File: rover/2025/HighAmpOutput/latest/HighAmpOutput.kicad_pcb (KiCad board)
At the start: 2 copper layers, 87.8 x 70.7 mm, 24 parts, among them J1 JST2_Pin, U1 EC5_Connector, U11 XT60PM-F, U12 XT60PM-F, U2 HSS-VN7004SLHTR, U3 XT60-F, U4 XT60-F, U5 XT60-F, U6 XT60-F, U7 XT60-F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

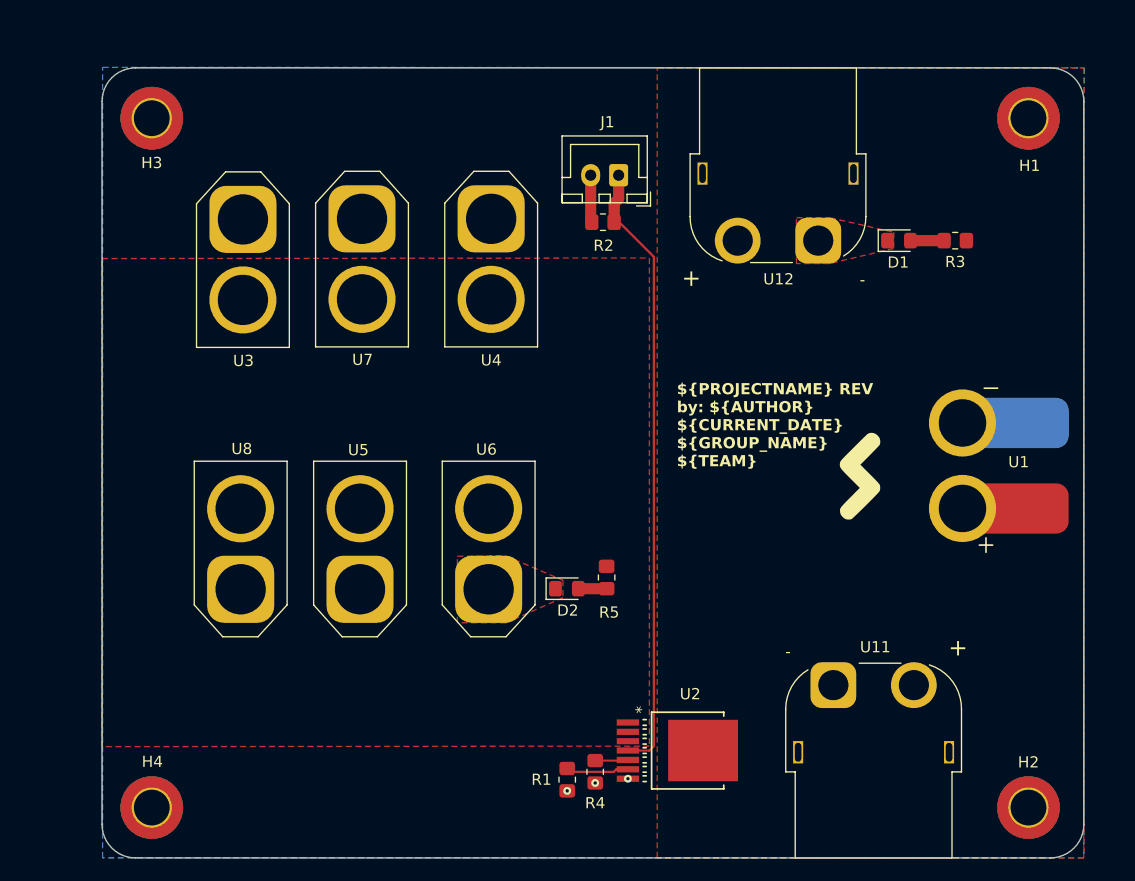
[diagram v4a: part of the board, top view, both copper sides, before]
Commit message: Correction PCB HighAmpOutput
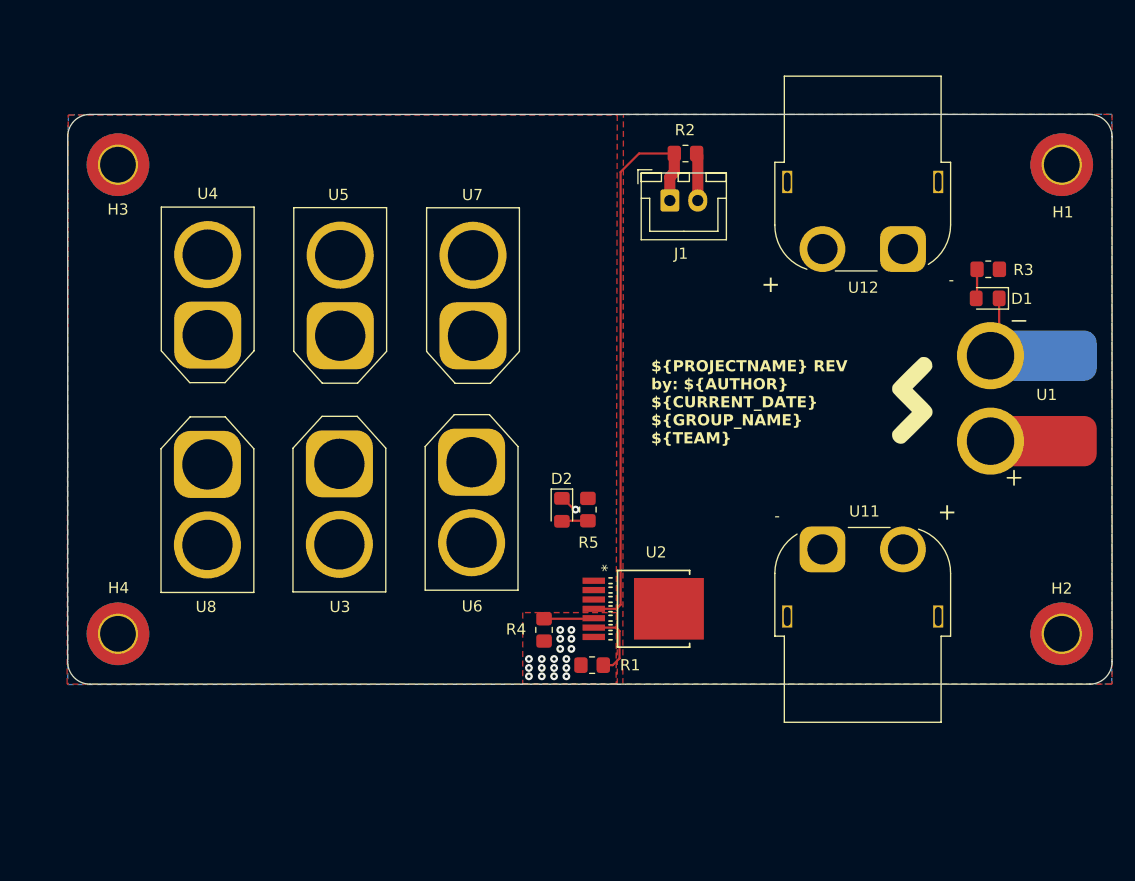
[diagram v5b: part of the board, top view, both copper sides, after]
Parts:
- moved U4 27.4 mm to (64.7, 77.5), turned to 90 degrees
- moved U3 23.5 mm to (76.5, 89.0)
- moved U5 22.7 mm to (76.5, 77.5)
- moved H4 15.8 mm to (56.7, 104.2)
- moved H2 15.8 mm to (141.1, 104.2)
- moved U7 14.4 mm to (88.4, 77.6), turned to 90 degrees
- moved R4 13.5 mm to (94.8, 103.9)
- moved U2 13.0 mm to (104.6, 102.0)
- moved U11 12.2 mm to (119.7, 96.7)
- moved U8 11.6 mm to (64.7, 89.1), turned to -90 degrees
- moved U6 11.5 mm to (88.3, 88.9), turned to -90 degrees
- moved R1 10.5 mm to (99.1, 107.0), turned to 180 degrees
- moved R2 9.60 mm to (107.4, 61.3), turned to 0 degrees
- moved D1 9.46 mm to (134.5, 74.2), turned to 180 degrees
- moved G*** 8.45 mm to (127.5, 83.1), turned to 0 degrees
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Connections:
- H1 pad 1: GND -> unconnected-(H1-Pad1)_2
- H2 pad 1: GND -> unconnected-(H2-Pad1)_2
- H3 pad 1: GND -> unconnected-(H3-Pad1)_1
- H4 pad 1: GND -> unconnected-(H4-Pad1)_1
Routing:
- net GND: track 4.05 -> 11.0 mm, vias 3 -> 19
- net Net-(U2-INPUT): track 55.4 -> 51.1 mm
- net Net-(U2-CS): track 2.95 -> 4.47 mm
- net Net-(U2-FR_DIAG): track 5.64 -> 6.58 mm
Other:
- board size 87.8 x 70.7 mm -> 93.4 x 51 mm

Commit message: Update HighAmpOutput.kicad_pcb
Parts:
- moved G*** 0.76 mm to (126.8, 83.1)
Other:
- board text added: "+24V"
- board text added: "+24V_I"
- board text added: "DDB"
- board text added: "HIGH_POWER_EN"
- board text added: "Sélecteur"
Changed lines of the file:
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@@
 		(tags "RC Connector XT60")
 		(property "Reference" "U12"
-			(at -3.55 3.45 0)
+			(at -3.026437 5.649081 0)
 			(layer "F.SilkS")
 			(effects
@@
 		)
 		(fp_text user "+"
-			(at -11.826437 3.149081 0)
+			(at -10.826437 3.149081 0)
 			(layer "F.SilkS")
 			(effects
@@
 		)
 		(fp_text user "-"
-			(at 4.323563 2.749081 0)
+			(at 3.973563 2.799081 0)
 			(layer "F.SilkS")
 			(effects
@@
 		(tags "mounting hole 3.2mm m3 din965")
 		(property "Reference" "H3"
-			(at 0 4 0)
+			(at 0 4.089081 0)
 			(layer "F.SilkS")
 			(effects
@@
 	(footprint "LOGO"
 		(layer "F.Cu")
-		(at 127.55 83.1)
+		(at 126.789123 83.114498)
 		(property "Reference" "G***"
 			(at 4.760877 0 0)
@@
 		(tags "RC Connector XT60")
 		(property "Reference" "U11"
-			(at -3.75 3.4 0)
+			(at -3.623563 5.510919 0)
 			(layer "F.SilkS")
 			(effects
@@
 		(tags "connector JST XH vertical")
 		(property "Reference" "J1"
-			(at 1 4.75 0)
+			(at 1.023563 6.089081 0)
 			(layer "F.SilkS")
 			(effects
@@
 		(tags "LED handsolder")
 		(property "Reference" "D2"
-			(at -2.775 0.025 180)
+			(at 2.825 -0.025 180)
 			(layer "F.SilkS")
 			(effects
@@
 		)
 	)
+	(gr_rect
+		(start 132.3 69.4)
+		(end 138.85 75.6)
+		(stroke
+			(width 0.1)
+			(type default)
+		)
+		(fill none)
+		(layer "F.SilkS")
+	)
+	(gr_rect
+		(start 94.5 90.75)
+		(end 100.6 96.95)
+		(stroke
+			(width 0.1)
+			(type default)
+		)
+		(fill none)
+		(layer "F.SilkS")
+	)
 	(gr_line
 		(start 145.576437 59.760919)
@@
 		(layer "User.1")
 	)
-	(gr_rect
-		(start 52.226436 57.810919)
-		(end 101.326436 108.710919)
-		(stroke
-			(width 0.1)
-			(type default)
-		)
-		(fill none)
-		(layer "User.1")
-	)
 	(gr_line
 		(start 181.4 139.4)
@@
 		(layer "User.4")
 	)
+	(gr_rect
+		(start 52.226436 57.810919)
+		(end 101.326436 108.710919)
+		(stroke
+			(width 0.1)
+			(type default)
+		)
+		(fill none)
+		(layer "User.4")
+	)
+	(gr_text "+24V_I "
+		(at 133.05 69.25 0)
+		(layer "F.SilkS" knockout)
+		(effects
+			(font
+				(size 1 1)
+				(thickness 0.1)
+			)
+			(justify left bottom)
+		)
+	)
+	(gr_text "DDB"
+		(at 120.8 93.9 0)
+		(layer "F.SilkS" knockout)
+		(effects
+			(font
+				(size 1.5 1.5)
+				(thickness 0.1875)
+			)
+			(justify left bottom)
+		)
+	)
+	(gr_text "Sélecteur"
+		(at 118.4 74.65 0)
+		(layer "F.SilkS" knockout)
+		(effects
+			(font
+				(size 1.5 1.5)
+				(thickness 0.1875)
+			)
+			(justify left bottom)
+		)
+	)
 	(gr_text "${PROJECTNAME} REV${REVISION}\nby: ${AUTHOR}\n${CURRENT_DATE}\n${GROUP_NAME}\n${TEAM}"
 		(at 104.35 87.3 0)
@@
 		)
 	)
+	(gr_text "HIGH_POWER_EN"
+		(at 103.05 70.45 0)
+		(layer "F.SilkS" knockout)
+		(effects
+			(font
+				(size 0.7 0.7)
+				(thickness 0.1)
+			)
+			(justify left bottom)
+		)
+	)
 	(gr_text "${PROJECTNAME} REV${REVISION}\nby: ${AUTHOR}\n${CURRENT_DATE}\n${GROUP_NAME}\n${TEAM}"
 		(at 30.4 38.2 0)
@@
 		)
 	)
+	(gr_text "+24V"
+		(at 95.3 90.7 0)
+		(layer "F.SilkS" knockout)
+		(effects
+			(font
+				(size 1 1)
+				(thickness 0.1)
+			)
+			(justify left bottom)
+		)
+	)
 	(dimension
 		(type aligned)
@@
 		)
 		(height -4.426436)
-		(gr_text "4,3000 mm"
+		(gr_text "4.3000 mm"
 			(at 82.55 83.65 90)
 			(layer "User.1")
@@
 		)
 		(height 12.83908)
-		(gr_text "93,4000 mm"
+		(gr_text "93.4000 mm"
 			(at 98.876437 118.399999 0)
 			(layer "User.1")
@@
 		)
 		(height -2.4)
-		(gr_text "36,1000 mm"
+		(gr_text "36.1000 mm"
 			(at 123.426437 85.160919 90)
 			(layer "User.1")
@@
 		)
 		(height -32.85)
-		(gr_text "57,7800 mm"
+		(gr_text "57.7800 mm"
 			(at 154.976437 83.230919 90)
 			(layer "User.1")
@@
 		)
 		(height 3.8)
-		(gr_text "33,0500 mm"
+		(gr_text "33.0500 mm"
 			(at 98.95 74.475 90)
 			(layer "User.1")
@@
 		)
 		(height 6.099999)
-		(gr_text "41,6500 mm"
+		(gr_text "41.6500 mm"
 			(at 110.95 91.7 90)
 			(layer "User.1")
@@
 		)
 		(height -10.85)
-		(gr_text "35,3500 mm"
+		(gr_text "35.3500 mm"
 			(at 150.776437 83.235919 90)
 			(layer "User.1")
@@
 		)
 		(height 2.681847)
-		(gr_text "12,7000 mm"
+		(gr_text "12.7000 mm"
 			(at 136.045781 64.313934 89.88721318)
 			(layer "User.1")
@@
 		)
 		(height -1.4)
-		(gr_text "25,6000 mm"
+		(gr_text "25.6000 mm"
 			(at 134.976437 95.660919 90)
 			(layer "User.1")
@@
 		)
 		(height -4.876436)
-		(gr_text "16,1000 mm"
+		(gr_text "16.1000 mm"
 			(at 82.35 66.010919 90)
 			(layer "User.1")
@@
 		)
 		(height 5.126436)
-		(gr_text "16,1500 mm"
+		(gr_text "16.1500 mm"
 			(at 81.85 100.435919 90)
 			(layer "User.1")
@@
 		)
 		(height 1.599999)
-		(gr_text "6,6000 mm"
+		(gr_text "6.6000 mm"
 			(at 93.7 96.15 90)
 			(layer "User.1")

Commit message: Done
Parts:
- removed the G*** at (53.6, 34.0)
- removed J1: JST2_Pin, RoverFootprint:2-pins-JST_XH_B2B-XH-A_1x02_P2.50mm_Vertical
- added J2: JST-PH-S2B, Connector_JST:JST_PH_B2B-PH-K_1x02_P2.00mm_Vertical, F.Cu at (106.4, 65.1)
- G***: moved to B.Cu
- moved G*** 26.7 mm to (100.1, 81.8), turned to 90 degrees
- moved H3 0.75 mm to (57.2, 62.8)
- moved D2 0.67 mm to (95.7, 93.1)
- moved H4 0.67 mm to (57.2, 103.8)
- moved H1 0.55 mm to (141.2, 62.8)
- moved H2 0.43 mm to (141.2, 103.8)
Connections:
- U11 pad : +24V_I -> (no net)
- U12 pad : +24V_I -> (no net)
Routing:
- net Net-(D2-A): track 2.33 -> 3.02 mm
- net GND: track 11.0 -> 11.6 mm
- net Net-(J2-Pin_1): track 51.1 -> 50.6 mm
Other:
- board size 93.4 x 51 mm -> 94 x 51 mm
